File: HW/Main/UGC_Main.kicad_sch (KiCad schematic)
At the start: 128 parts, among them J1 Rumble, J13 503480-0640, J2 LT, J3 RT, J4 Conn_01x06_Pin, J5 UJ31-CH-G1-SMT-TR, Q1 MMBT3904, Q2 MMBT3904, Q3 BSS138DW, Q4 BSS138DW, Q5 Q_NMOS_GSD, Q6 Q_PMOS_GDS, Q7 Q_NMOS_GSD, SW1 1TS026A-1000-0550, SW1 SW_Push, SW10 SW_Push, SW11 SW_Push, SW12 SW_Push, SW13 SW_Push, SW14 TS09-63-25-R-260-SMT, SW2 SW_Push, SW3 SW_Push, SW4 SW_Push, SW5 SW_Push, SW6 GL18_SW, SW7 SW_Push, SW8 SW_Push, SW9 TS09-63-25-R-260-SMT, U1 ESP32-PICO-MINI-02, U10 ST_LSM6, U11 BQ25180, U12 CH340K, U13 PI3USB4000A, U2 GD25Q80EEIGR, U2 GH39F (Hall SOT23), U3 GH39F (Hall SOT23), U4 TPS630001RCR, U5 ST_LSM6, U6 MCP3002, U7 MCP3002, U8 RP2040, Y1 Crystal_GND3

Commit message: Update board
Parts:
- SW1, SW2, SW3, SW4: footprint hhl:progcc_bpad -> hhl:ring_pad
- SW10, SW11, SW12, SW13: footprint hhl:progcc_dpad -> hhl:ring_dpad
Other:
- moved on the sheet: C1, C2, C24, C3, D10, D9, F1, L5, R3, TP5, U4

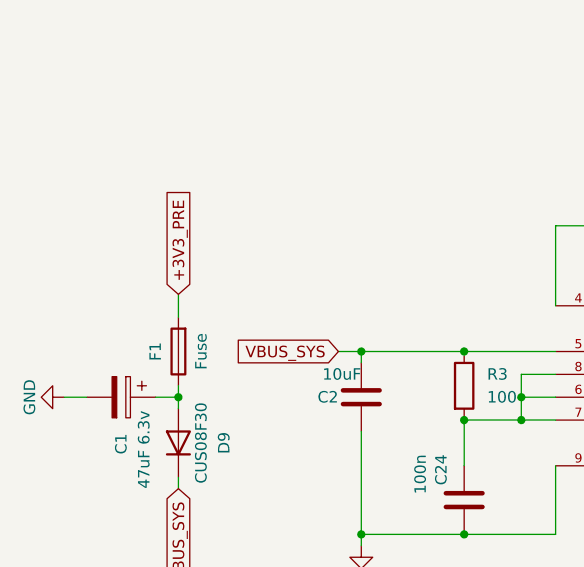
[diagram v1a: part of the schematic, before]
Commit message: 5.17.2024 Updates
- Fix PCB with fuse removal (3.3 undervolted)
- Fixes for N64 mode
- Fixes for GameCube mode + new input mode support for more titles
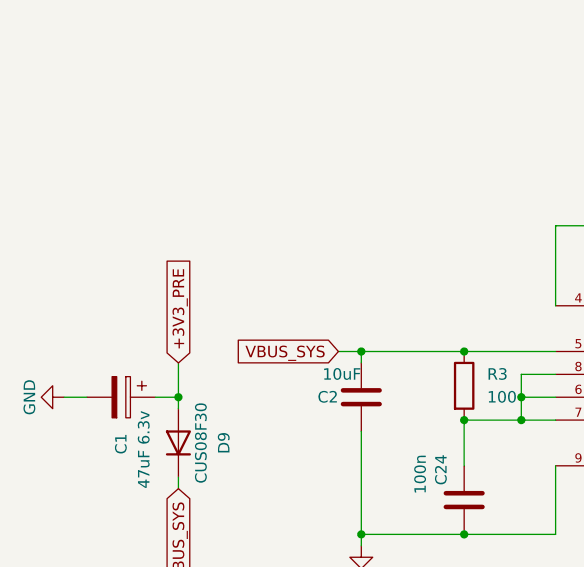
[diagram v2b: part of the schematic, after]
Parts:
- removed F1: Fuse, Fuse:Fuse_1206_3216Metric_Pad1.42x1.75mm_HandSolder, symbol Device:Fuse
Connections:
- net +3V3_PRE: now also C1.1, D9.2 (A)
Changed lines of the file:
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@@
     (stroke (width 0) (type default))
   )
-  (wire (pts (xy -105.41 90.17) (xy -105.41 91.44))
+  (wire (pts (xy -105.41 87.63) (xy -105.41 91.44))
     (stroke (width 0) (type default))
   )
@@
     (stroke (width 0) (type default))
   )
-  (wire (pts (xy -105.41 80.01) (xy -105.41 82.55))
-    (stroke (width 0) (type default))
-  )
   (wire (pts (xy 250.19 196.85) (xy 251.46 196.85))
     (stroke (width 0) (type default))
@@
     )
   )
-  (global_label "+3V3_PRE" (shape input) (at -105.41 80.01 90) (fields_autoplaced)
+  (global_label "+3V3_PRE" (shape input) (at -105.41 87.63 90) (fields_autoplaced)
     (effects (font (size 1.27 1.27)) (justify left))
-    (property "Intersheetrefs" "${INTERSHEET_REFS}" (at -105.41 67.2882 90)
+    (property "Intersheetrefs" "${INTERSHEET_REFS}" (at -105.41 74.9082 90)
       (effects (font (size 1.27 1.27)) (justify left) hide)
     )
@@
         )
       )
-    )
-  )
-  (symbol (lib_id "Device:Fuse") (at -105.41 86.36 180) (unit 1)
-    (in_bom yes) (on_board yes) (dnp no)
-    (property "Reference" "F1" (at -107.95 86.36 90)
-      (effects (font (size 1.27 1.27)))
-    )
-    (property "Value" "Fuse" (at -102.87 86.36 90)
-      (effects (font (size 1.27 1.27)))
-    )
-    (property "Footprint" "Fuse:Fuse_1206_3216Metric_Pad1.42x1.75mm_HandSolder" (at -103.632 86.36 90)
-      (effects (font (size 1.27 1.27)) hide)
-    )
-    (property "Datasheet" "~" (at -105.41 86.36 0)
-      (effects (font (size 1.27 1.27)) hide)
-    )
-    (property "LCSC" "C69680" (at -105.41 86.36 0)
-      (effects (font (size 1.27 1.27)) hide)
-    )
-    (property "MPN" "" (at -105.41 86.36 0)
-      (effects (font (size 1.27 1.27)) hide)
-    )
-    (property "Manufacturer" "" (at -105.41 86.36 0)
-      (effects (font (size 1.27 1.27)) hide)
-    )
-    (pin "1")
-    (pin "2")
-    (instances
-      (project "GCP-2"
-        (path "/066be9b8-34d2-4336-ae00-5e5ce007fbe1"
-          (reference "F1") (unit 1)
-        )
-      )
-      (project "UGC_Main"
-        (path "/5d3b68ed-8c8a-4ed0-8f2b-63049c253646"
-          (reference "F2") (unit 1)
-        )
-      )
-      (project "procon_gcc_main_pcb"
-        (path "/9ec9c1c0-f5f6-4920-ad47-c5d4aa989114"
-          (reference "F2") (unit 1)
-        )
-      )
